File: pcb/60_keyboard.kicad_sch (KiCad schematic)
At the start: 0 parts

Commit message: commited
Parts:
- added SW1, SW10, SW11, SW12, SW13, SW14, SW15, SW16, SW17, SW18, SW19, SW2, SW20, SW21, SW22, SW23, SW24, SW25, SW26, SW27, SW28, SW29, SW3, SW30, SW31, SW32, SW33, SW34, SW35, SW36, SW37, SW38, SW39, SW4, SW40, SW41, SW42, SW43, SW44, SW45, SW46, SW47, SW48, SW49, SW5, SW50, SW51, SW52, SW53, SW54, SW6, SW7, SW8, SW9: SW_MEC_5G, symbol Switch:SW_MEC_5G
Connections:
- new net: SW38.1 (A), SW38.2 (A)
- new net: SW38.3 (B), SW38.4 (B)
- new net: SW48.1 (A), SW48.2 (A)
- new net: SW48.3 (B), SW48.4 (B)
- new net: SW13.1 (A), SW13.2 (A)
- new net: SW13.3 (B), SW13.4 (B)
- new net: SW12.1 (A), SW12.2 (A)
- new net: SW12.3 (B), SW12.4 (B)
- new net: SW20.1 (A), SW20.2 (A)
- new net: SW20.3 (B), SW20.4 (B)
- new net: SW19.1 (A), SW19.2 (A)
- new net: SW19.3 (B), SW19.4 (B)
- new net: SW45.1 (A), SW45.2 (A)
- new net: SW45.3 (B), SW45.4 (B)
- new net: SW51.1 (A), SW51.2 (A)
- new net: SW51.3 (B), SW51.4 (B)
- new net: SW23.1 (A), SW23.2 (A)
- new net: SW23.3 (B), SW23.4 (B)
- new net: SW29.1 (A), SW29.2 (A)
- new net: SW29.3 (B), SW29.4 (B)
- new net: SW24.1 (A), SW24.2 (A)
- new net: SW24.3 (B), SW24.4 (B)
- new net: SW40.1 (A), SW40.2 (A)
- new net: SW40.3 (B), SW40.4 (B)
- new net: SW50.1 (A), SW50.2 (A)
- new net: SW50.3 (B), SW50.4 (B)
- new net: SW9.1 (A), SW9.2 (A)
- new net: SW9.3 (B), SW9.4 (B)
- new net: SW30.1 (A), SW30.2 (A)
- new net: SW30.3 (B), SW30.4 (B)
- new net: SW27.1 (A), SW27.2 (A)
- new net: SW27.3 (B), SW27.4 (B)
- new net: SW7.1 (A), SW7.2 (A)
- new net: SW7.3 (B), SW7.4 (B)
- new net: SW46.1 (A), SW46.2 (A)
- new net: SW46.3 (B), SW46.4 (B)
- new net: SW34.1 (A), SW34.2 (A)
- new net: SW34.3 (B), SW34.4 (B)
- new net: SW54.1 (A), SW54.2 (A)
- new net: SW54.3 (B), SW54.4 (B)
- new net: SW31.1 (A), SW31.2 (A)
- new net: SW31.3 (B), SW31.4 (B)
- new net: SW14.1 (A), SW14.2 (A)
- new net: SW14.3 (B), SW14.4 (B)
- new net: SW52.1 (A), SW52.2 (A)
- new net: SW52.3 (B), SW52.4 (B)
- new net: SW42.1 (A), SW42.2 (A)
- new net: SW42.3 (B), SW42.4 (B)
- new net: SW35.1 (A), SW35.2 (A)
- new net: SW35.3 (B), SW35.4 (B)
- new net: SW22.1 (A), SW22.2 (A)
- new net: SW22.3 (B), SW22.4 (B)
- new net: SW41.1 (A), SW41.2 (A)
- new net: SW41.3 (B), SW41.4 (B)
- new net: SW5.1 (A), SW5.2 (A)
- new net: SW5.3 (B), SW5.4 (B)
- new net: SW2.1 (A), SW2.2 (A)
- new net: SW2.3 (B), SW2.4 (B)
- new net: SW28.1 (A), SW28.2 (A)
- new net: SW28.3 (B), SW28.4 (B)
- new net: SW33.1 (A), SW33.2 (A)
- new net: SW33.3 (B), SW33.4 (B)
- new net: SW47.1 (A), SW47.2 (A)
- new net: SW47.3 (B), SW47.4 (B)
- new net: SW39.1 (A), SW39.2 (A)
- new net: SW39.3 (B), SW39.4 (B)
- new net: SW21.1 (A), SW21.2 (A)
- new net: SW21.3 (B), SW21.4 (B)
- new net: SW16.1 (A), SW16.2 (A)
- new net: SW16.3 (B), SW16.4 (B)
- new net: SW8.1 (A), SW8.2 (A)
- new net: SW8.3 (B), SW8.4 (B)
- new net: SW4.1 (A), SW4.2 (A)
- new net: SW4.3 (B), SW4.4 (B)
- new net: SW43.1 (A), SW43.2 (A)
- new net: SW43.3 (B), SW43.4 (B)
- new net: SW11.1 (A), SW11.2 (A)
- new net: SW11.3 (B), SW11.4 (B)
- new net: SW53.1 (A), SW53.2 (A)
- new net: SW53.3 (B), SW53.4 (B)
- new net: SW37.1 (A), SW37.2 (A)
- new net: SW37.3 (B), SW37.4 (B)
- new net: SW17.1 (A), SW17.2 (A)
- new net: SW17.3 (B), SW17.4 (B)
- new net: SW10.1 (A), SW10.2 (A)
- new net: SW10.3 (B), SW10.4 (B)
- new net: SW49.1 (A), SW49.2 (A)
- new net: SW49.3 (B), SW49.4 (B)
- new net: SW6.1 (A), SW6.2 (A)
- new net: SW6.3 (B), SW6.4 (B)
- new net: SW15.1 (A), SW15.2 (A)
- new net: SW15.3 (B), SW15.4 (B)
- new net: SW18.1 (A), SW18.2 (A)
- new net: SW18.3 (B), SW18.4 (B)
- new net: SW25.1 (A), SW25.2 (A)
- new net: SW25.3 (B), SW25.4 (B)
- new net: SW3.1 (A), SW3.2 (A)
- new net: SW3.3 (B), SW3.4 (B)
- new net: SW44.1 (A), SW44.2 (A)
- new net: SW44.3 (B), SW44.4 (B)
- new net: SW1.1 (A), SW1.2 (A)
- new net: SW1.3 (B), SW1.4 (B)
- new net: SW36.1 (A), SW36.2 (A)
- new net: SW36.3 (B), SW36.4 (B)
- new net: SW26.1 (A), SW26.2 (A)
- new net: SW26.3 (B), SW26.4 (B)
- new net: SW32.1 (A), SW32.2 (A)
- new net: SW32.3 (B), SW32.4 (B)

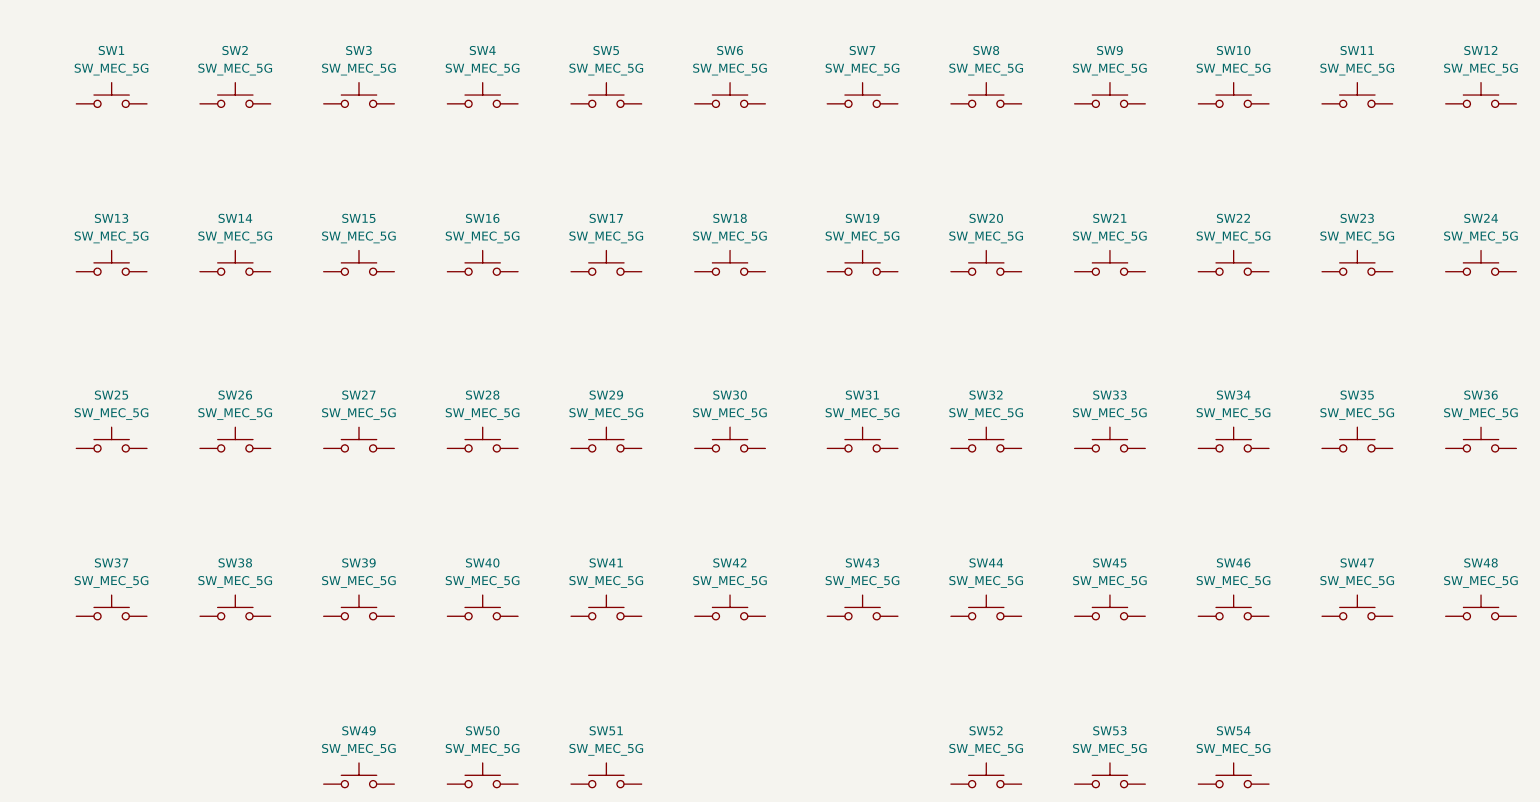
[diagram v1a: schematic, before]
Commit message: Added main parts
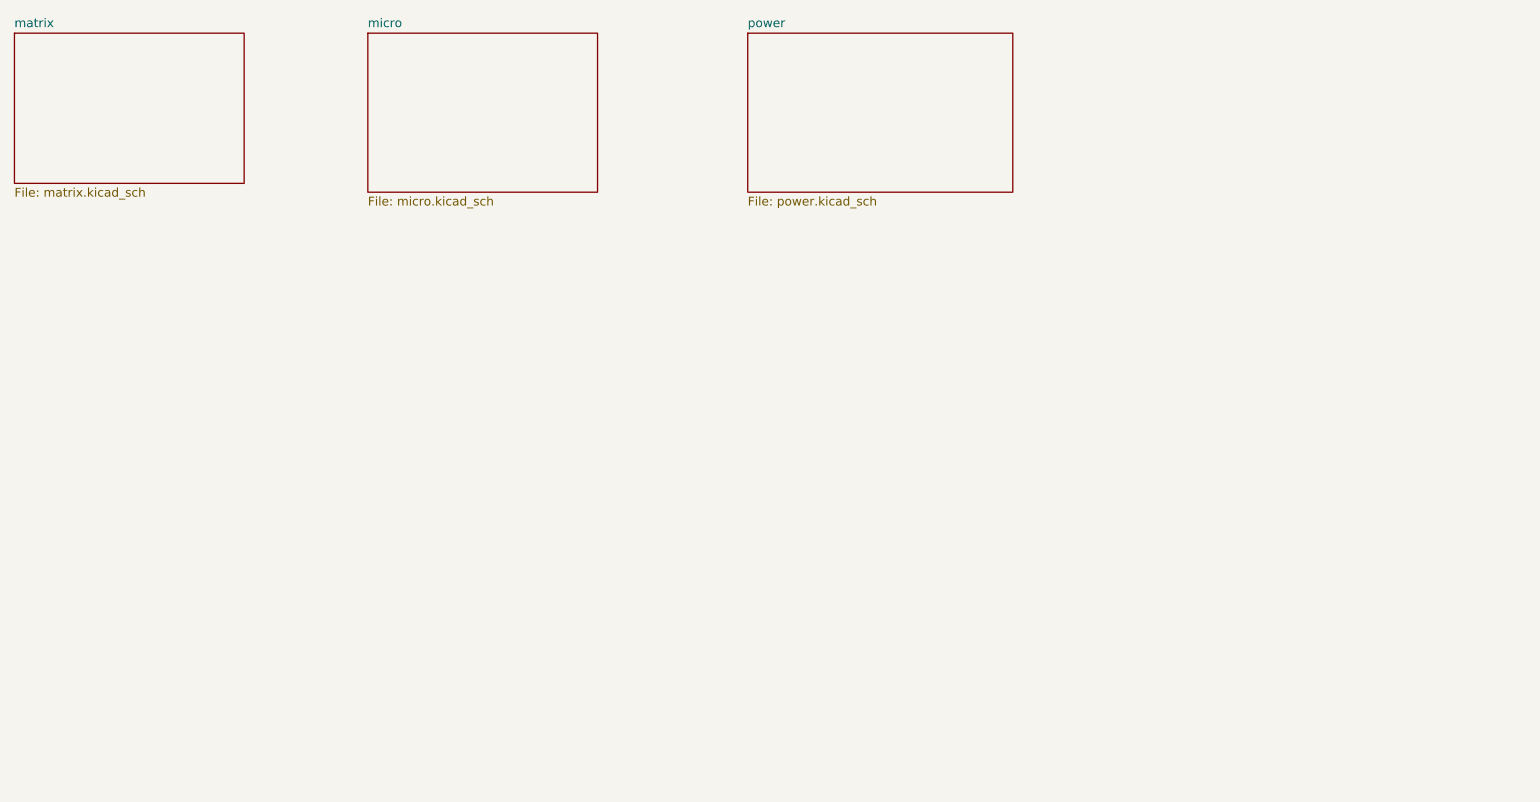
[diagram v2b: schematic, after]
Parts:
- removed SW1, SW10, SW11, SW12, SW13, SW14, SW15, SW16, SW17, SW18, SW19, SW2, SW20, SW21, SW22, SW23, SW24, SW25, SW26, SW27, SW28, SW29, SW3, SW30, SW31, SW32, SW33, SW34, SW35, SW36, SW37, SW38, SW39, SW4, SW40, SW41, SW42, SW43, SW44, SW45, SW46, SW47, SW48, SW49, SW5, SW50, SW51, SW52, SW53, SW54, SW6, SW7, SW8, SW9: SW_MEC_5G, symbol Switch:SW_MEC_5G
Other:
- added sheet matrix (matrix.kicad_sch)
- added sheet micro (micro.kicad_sch)
- added sheet power (power.kicad_sch)
